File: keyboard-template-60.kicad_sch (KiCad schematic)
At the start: 171 parts, among them J1 USB_C_Receptacle_USB2.0, J2 Conn_01x04, SW1 SW_Reset, U1 ATmega32U4-A, U2 SRV05-4, Y1 16MHz

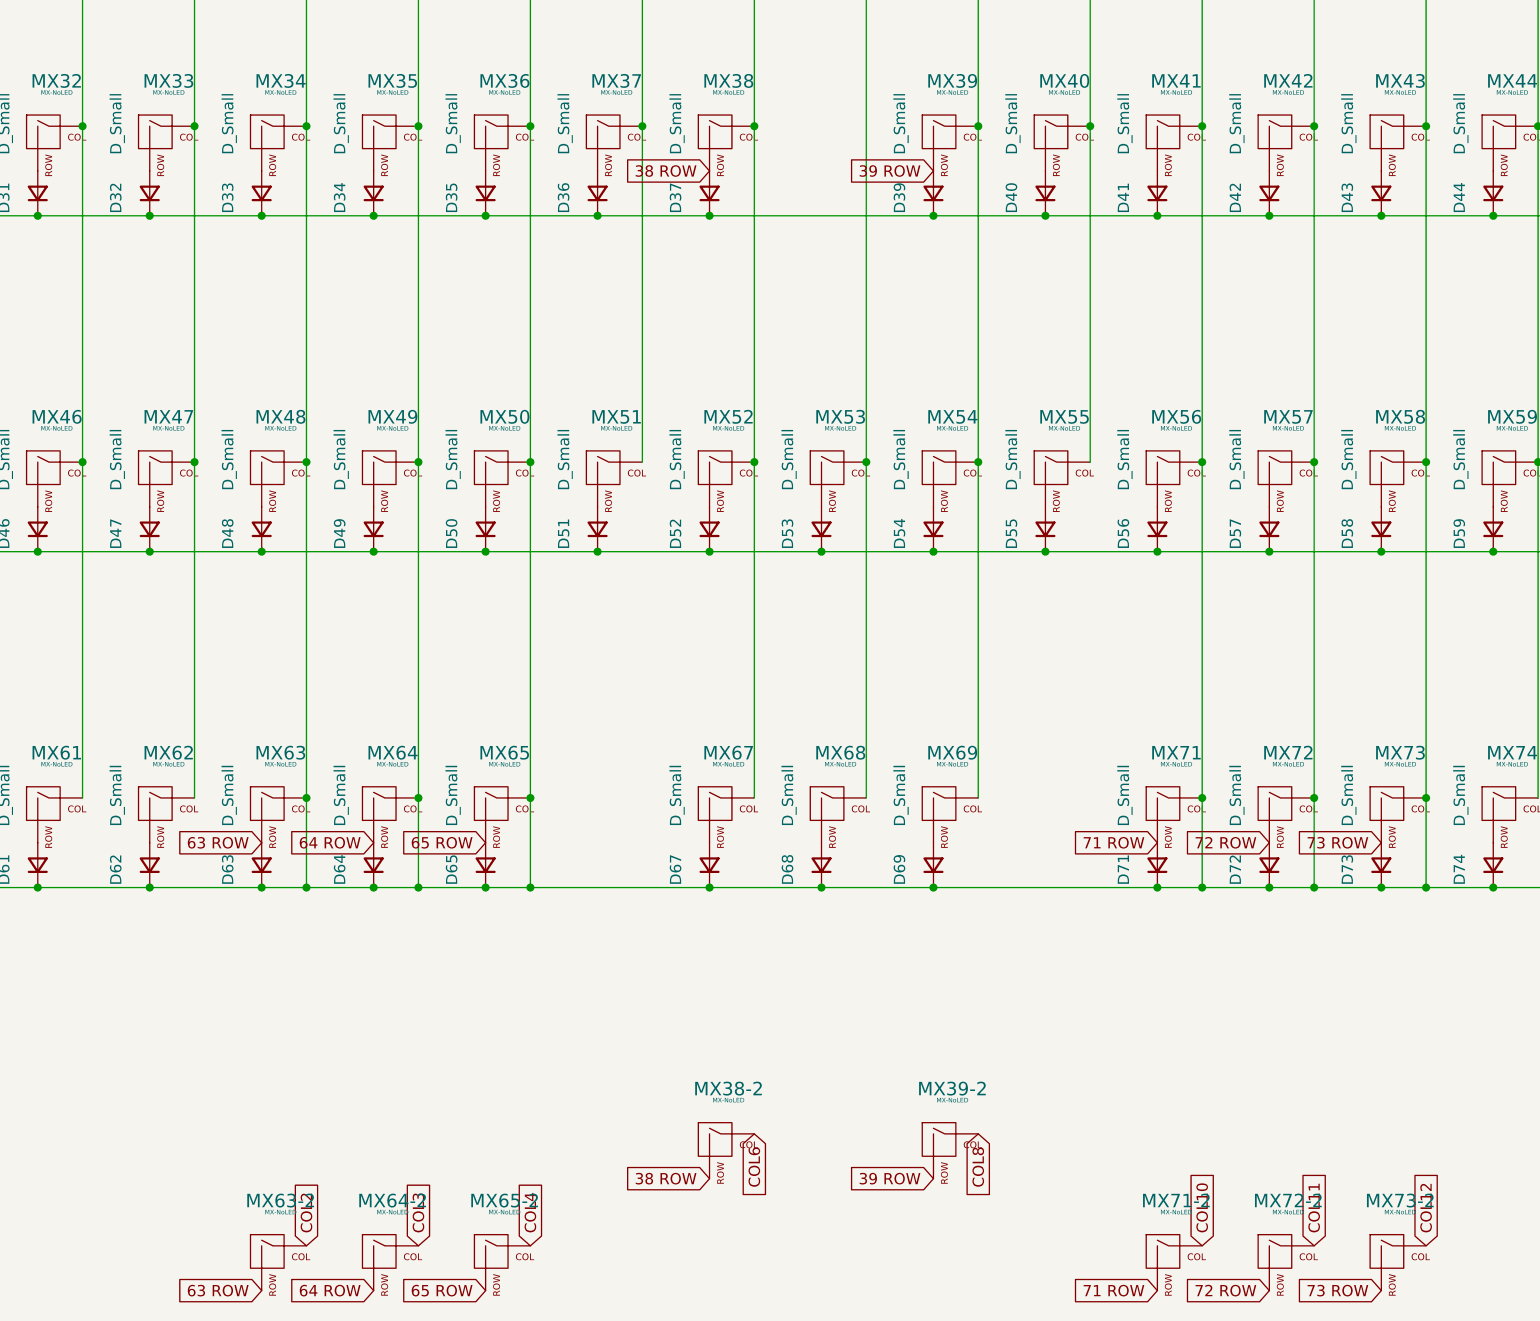
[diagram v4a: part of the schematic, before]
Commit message: Refactor the alternative switch positions
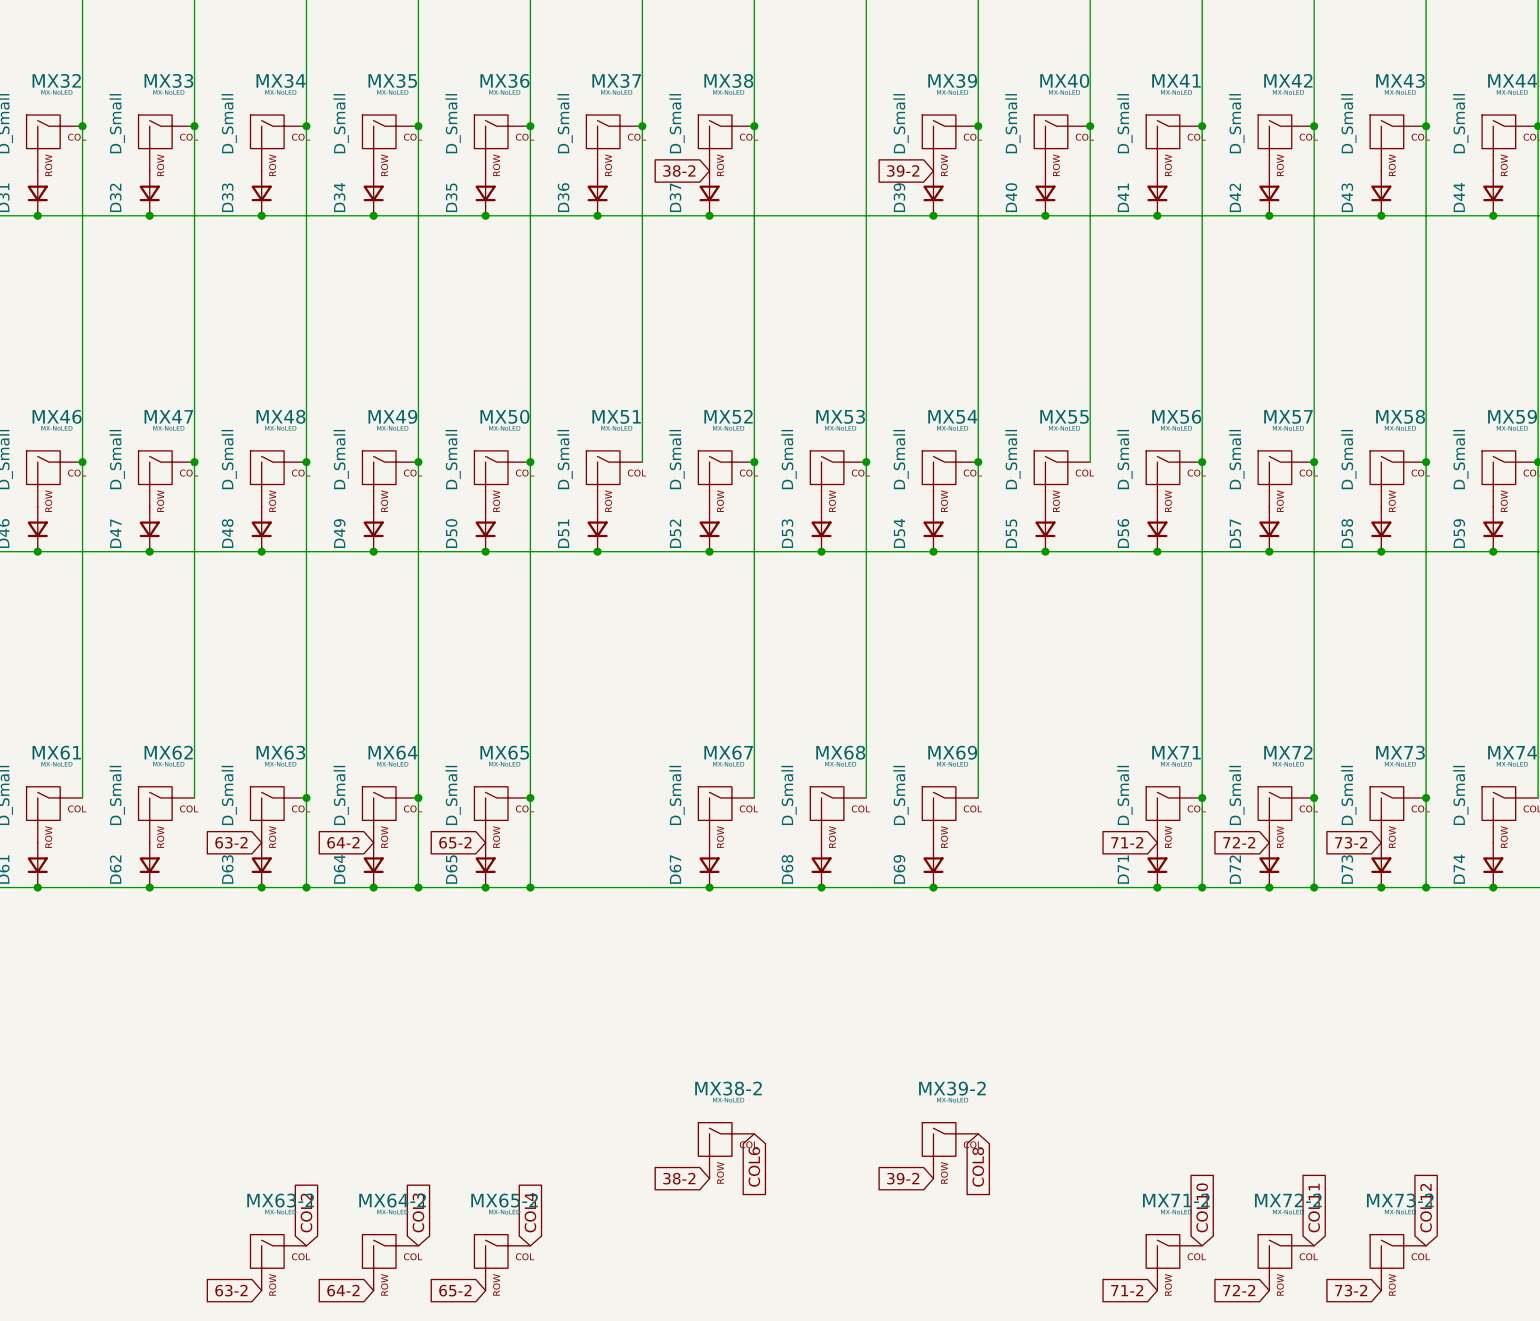
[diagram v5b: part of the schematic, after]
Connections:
- net 38 ROW renamed 38-2
- net 39 ROW renamed 39-2
- net 63 ROW renamed 63-2
- net 64 ROW renamed 64-2
- net 65 ROW renamed 65-2
- net 71 ROW renamed 71-2
- net 72 ROW renamed 72-2
- net 73 ROW renamed 73-2
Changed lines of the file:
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@@
     (stroke (width 0) (type default) (color 0 0 0 0))
   )
-  (global_label "65 ROW" (shape input) (at 102.87 209.55 180) (fields_autoplaced)
-    (effects (font (size 1.27 1.27)) (justify right))
-    (property "Intersheet References" "${INTERSHEET_REFS}" (id 0) (at 93.0183 209.4706 0)
+  (global_label "65-2" (shape input) (at 102.87 209.55 180) (fields_autoplaced)
+    (effects (font (size 1.27 1.27)) (justify right))
+    (property "Intersheet References" "${INTERSHEET_REFS}" (id 0) (at 95.2559 209.4706 0)
       (effects (font (size 1.27 1.27)) (justify right) hide)
     )
@@
     )
   )
-  (global_label "71 ROW" (shape input) (at 179.07 209.55 180) (fields_autoplaced)
-    (effects (font (size 1.27 1.27)) (justify right))
-    (property "Intersheet References" "${INTERSHEET_REFS}" (id 0) (at 169.2183 209.4706 0)
-      (effects (font (size 1.27 1.27)) (justify right) hide)
-    )
-  )
-  (global_label "63 ROW" (shape input) (at 77.47 209.55 180) (fields_autoplaced)
-    (effects (font (size 1.27 1.27)) (justify right))
-    (property "Intersheet References" "${INTERSHEET_REFS}" (id 0) (at 67.6183 209.4706 0)
+  (global_label "71-2" (shape input) (at 179.07 209.55 180) (fields_autoplaced)
+    (effects (font (size 1.27 1.27)) (justify right))
+    (property "Intersheet References" "${INTERSHEET_REFS}" (id 0) (at 171.4559 209.4706 0)
+      (effects (font (size 1.27 1.27)) (justify right) hide)
+    )
+  )
+  (global_label "63-2" (shape input) (at 77.47 209.55 180) (fields_autoplaced)
+    (effects (font (size 1.27 1.27)) (justify right))
+    (property "Intersheet References" "${INTERSHEET_REFS}" (id 0) (at 69.8559 209.4706 0)
       (effects (font (size 1.27 1.27)) (justify right) hide)
     )
@@
     )
   )
-  (global_label "73 ROW" (shape input) (at 204.47 209.55 180) (fields_autoplaced)
-    (effects (font (size 1.27 1.27)) (justify right))
-    (property "Intersheet References" "${INTERSHEET_REFS}" (id 0) (at 194.6183 209.4706 0)
+  (global_label "73-2" (shape input) (at 204.47 209.55 180) (fields_autoplaced)
+    (effects (font (size 1.27 1.27)) (justify right))
+    (property "Intersheet References" "${INTERSHEET_REFS}" (id 0) (at 196.8559 209.4706 0)
       (effects (font (size 1.27 1.27)) (justify right) hide)
     )
@@
     )
   )
-  (global_label "71 ROW" (shape input) (at 179.07 260.35 180) (fields_autoplaced)
-    (effects (font (size 1.27 1.27)) (justify right))
-    (property "Intersheet References" "${INTERSHEET_REFS}" (id 0) (at 169.2183 260.2706 0)
+  (global_label "71-2" (shape input) (at 179.07 260.35 180) (fields_autoplaced)
+    (effects (font (size 1.27 1.27)) (justify right))
+    (property "Intersheet References" "${INTERSHEET_REFS}" (id 0) (at 171.4559 260.2706 0)
       (effects (font (size 1.27 1.27)) (justify right) hide)
     )
@@
     )
   )
-  (global_label "63 ROW" (shape input) (at 77.47 260.35 180) (fields_autoplaced)
-    (effects (font (size 1.27 1.27)) (justify right))
-    (property "Intersheet References" "${INTERSHEET_REFS}" (id 0) (at 67.6183 260.2706 0)
+  (global_label "63-2" (shape input) (at 77.47 260.35 180) (fields_autoplaced)
+    (effects (font (size 1.27 1.27)) (justify right))
+    (property "Intersheet References" "${INTERSHEET_REFS}" (id 0) (at 69.8559 260.2706 0)
       (effects (font (size 1.27 1.27)) (justify right) hide)
     )
@@
     )
   )
-  (global_label "64 ROW" (shape input) (at 90.17 209.55 180) (fields_autoplaced)
-    (effects (font (size 1.27 1.27)) (justify right))
-    (property "Intersheet References" "${INTERSHEET_REFS}" (id 0) (at 80.3183 209.4706 0)
+  (global_label "64-2" (shape input) (at 90.17 209.55 180) (fields_autoplaced)
+    (effects (font (size 1.27 1.27)) (justify right))
+    (property "Intersheet References" "${INTERSHEET_REFS}" (id 0) (at 82.5559 209.4706 0)
       (effects (font (size 1.27 1.27)) (justify right) hide)
     )
@@
     )
   )
-  (global_label "39 ROW" (shape input) (at 153.67 133.35 180) (fields_autoplaced)
-    (effects (font (size 1.27 1.27)) (justify right))
-    (property "Intersheet References" "${INTERSHEET_REFS}" (id 0) (at 143.8183 133.2706 0)
+  (global_label "39-2" (shape input) (at 153.67 133.35 180) (fields_autoplaced)
+    (effects (font (size 1.27 1.27)) (justify right))
+    (property "Intersheet References" "${INTERSHEET_REFS}" (id 0) (at 146.0559 133.2706 0)
       (effects (font (size 1.27 1.27)) (justify right) hide)
     )
@@
     )
   )
-  (global_label "38 ROW" (shape input) (at 128.27 247.65 180) (fields_autoplaced)
-    (effects (font (size 1.27 1.27)) (justify right))
-    (property "Intersheet References" "${INTERSHEET_REFS}" (id 0) (at 118.4183 247.5706 0)
+  (global_label "38-2" (shape input) (at 128.27 247.65 180) (fields_autoplaced)
+    (effects (font (size 1.27 1.27)) (justify right))
+    (property "Intersheet References" "${INTERSHEET_REFS}" (id 0) (at 120.6559 247.5706 0)
       (effects (font (size 1.27 1.27)) (justify right) hide)
     )
@@
     )
   )
-  (global_label "65 ROW" (shape input) (at 102.87 260.35 180) (fields_autoplaced)
-    (effects (font (size 1.27 1.27)) (justify right))
-    (property "Intersheet References" "${INTERSHEET_REFS}" (id 0) (at 93.0183 260.2706 0)
+  (global_label "65-2" (shape input) (at 102.87 260.35 180) (fields_autoplaced)
+    (effects (font (size 1.27 1.27)) (justify right))
+    (property "Intersheet References" "${INTERSHEET_REFS}" (id 0) (at 95.2559 260.2706 0)
       (effects (font (size 1.27 1.27)) (justify right) hide)
     )
@@
     )
   )
-  (global_label "39 ROW" (shape input) (at 153.67 247.65 180) (fields_autoplaced)
-    (effects (font (size 1.27 1.27)) (justify right))
-    (property "Intersheet References" "${INTERSHEET_REFS}" (id 0) (at 143.8183 247.5706 0)
+  (global_label "39-2" (shape input) (at 153.67 247.65 180) (fields_autoplaced)
+    (effects (font (size 1.27 1.27)) (justify right))
+    (property "Intersheet References" "${INTERSHEET_REFS}" (id 0) (at 146.0559 247.5706 0)
       (effects (font (size 1.27 1.27)) (justify right) hide)
     )
@@
     )
   )
-  (global_label "72 ROW" (shape input) (at 191.77 209.55 180) (fields_autoplaced)
-    (effects (font (size 1.27 1.27)) (justify right))
-    (property "Intersheet References" "${INTERSHEET_REFS}" (id 0) (at 181.9183 209.4706 0)
+  (global_label "72-2" (shape input) (at 191.77 209.55 180) (fields_autoplaced)
+    (effects (font (size 1.27 1.27)) (justify right))
+    (property "Intersheet References" "${INTERSHEET_REFS}" (id 0) (at 184.1559 209.4706 0)
       (effects (font (size 1.27 1.27)) (justify right) hide)
     )
@@
     )
   )
-  (global_label "73 ROW" (shape input) (at 204.47 260.35 180) (fields_autoplaced)
-    (effects (font (size 1.27 1.27)) (justify right))
-    (property "Intersheet References" "${INTERSHEET_REFS}" (id 0) (at 194.6183 260.2706 0)
+  (global_label "73-2" (shape input) (at 204.47 260.35 180) (fields_autoplaced)
+    (effects (font (size 1.27 1.27)) (justify right))
+    (property "Intersheet References" "${INTERSHEET_REFS}" (id 0) (at 196.8559 260.2706 0)
       (effects (font (size 1.27 1.27)) (justify right) hide)
     )
@@
     )
   )
-  (global_label "64 ROW" (shape input) (at 90.17 260.35 180) (fields_autoplaced)
-    (effects (font (size 1.27 1.27)) (justify right))
-    (property "Intersheet References" "${INTERSHEET_REFS}" (id 0) (at 80.3183 260.2706 0)
+  (global_label "64-2" (shape input) (at 90.17 260.35 180) (fields_autoplaced)
+    (effects (font (size 1.27 1.27)) (justify right))
+    (property "Intersheet References" "${INTERSHEET_REFS}" (id 0) (at 82.5559 260.2706 0)
       (effects (font (size 1.27 1.27)) (justify right) hide)
     )
@@
     )
   )
-  (global_label "38 ROW" (shape input) (at 128.27 133.35 180) (fields_autoplaced)
-    (effects (font (size 1.27 1.27)) (justify right))
-    (property "Intersheet References" "${INTERSHEET_REFS}" (id 0) (at 118.4183 133.2706 0)
+  (global_label "38-2" (shape input) (at 128.27 133.35 180) (fields_autoplaced)
+    (effects (font (size 1.27 1.27)) (justify right))
+    (property "Intersheet References" "${INTERSHEET_REFS}" (id 0) (at 120.6559 133.2706 0)
       (effects (font (size 1.27 1.27)) (justify right) hide)
     )
@@
     )
   )
-  (global_label "72 ROW" (shape input) (at 191.77 260.35 180) (fields_autoplaced)
-    (effects (font (size 1.27 1.27)) (justify right))
-    (property "Intersheet References" "${INTERSHEET_REFS}" (id 0) (at 181.9183 260.2706 0)
-      (effects (font (size 1.27 1.27)) (justify right) hide)
-    )
+  (global_label "72-2" (shape input) (at 191.77 260.35 180) (fields_autoplaced)
+    (effects (font (size 1.27 1.27)) (justify right))
+    (property "Intersheet References" "${INTERSHEET_REFS}" (id 0) (at 184.1559 260.2706 0)
+      (effects (font (size 1.27 1.27)) (justify right) hide)
+    )

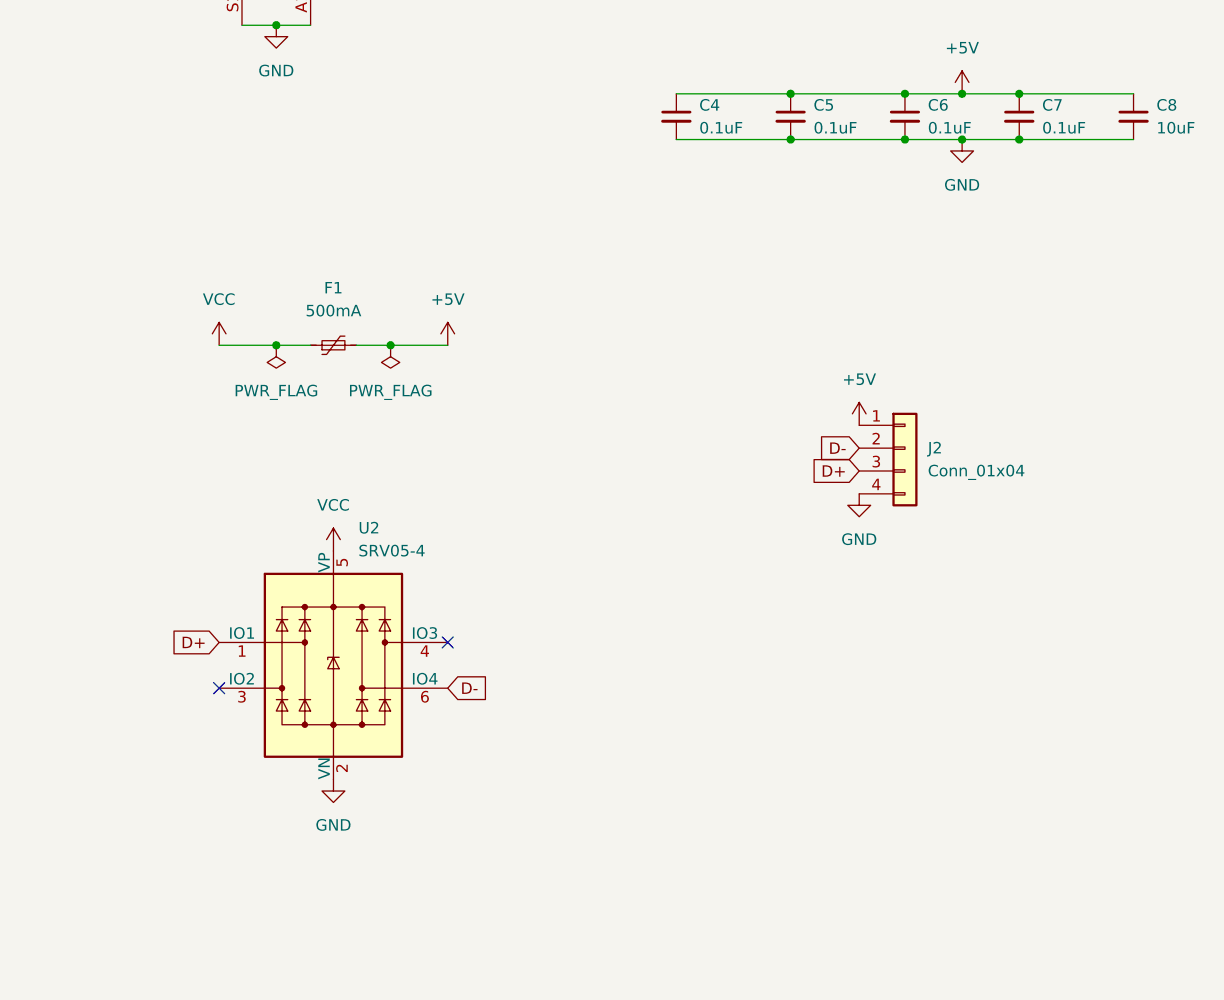
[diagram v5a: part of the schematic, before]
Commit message: Swapped the JST connector
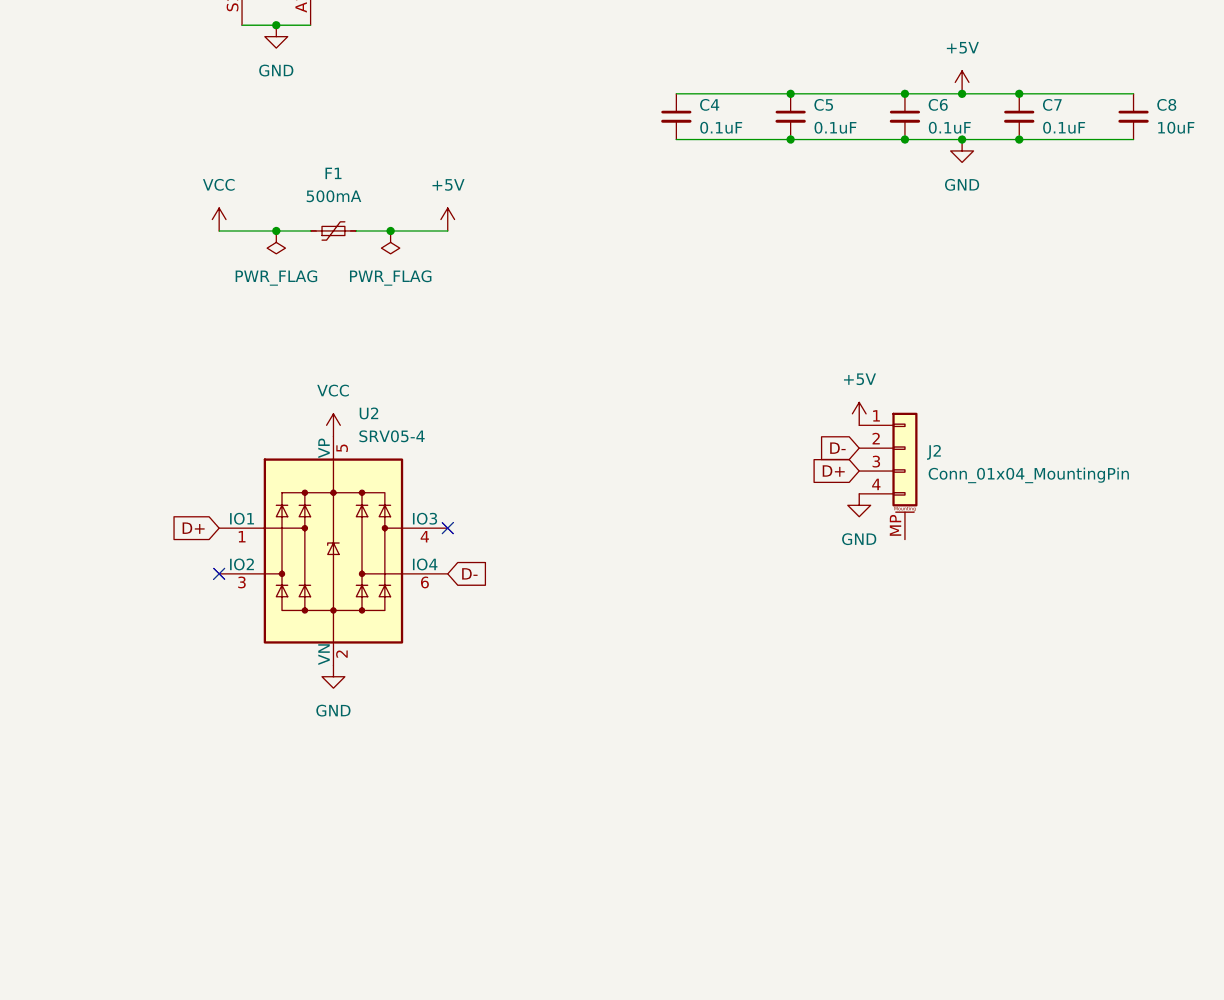
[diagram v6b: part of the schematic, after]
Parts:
- removed J2: Conn_01x04, symbol Connector_Generic:Conn_01x04
- added J2: Conn_01x04_MountingPin, symbol Connector_Generic_MountingPin:Conn_01x04_MountingPin
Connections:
- net +5V: now also J2.1 (Pin_1)
- net D+: now also J2.3 (Pin_3)
- net D-: now also J2.2 (Pin_2)
- net GND: now also J2.4 (Pin_4)
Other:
- moved on the sheet: F1, U2
